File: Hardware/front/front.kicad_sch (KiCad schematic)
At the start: 31 parts, among them J101 Conn_02x10_Odd_Even, J102 Conn_02x08_Odd_Even, SW101 Alps EC11E, SW102 C&K-D6R-Illuminated, SW103 B3W-9002-Y1C, SW104 B3W-9002-Y1C, SW105 B3W-9002-Y1C, SW106 B3W-9002-Y1C, SW107 B3W-9000-RHG2C, U101 XRA1203, U102 AT24CS32-SSHM, U103 PCA9955B

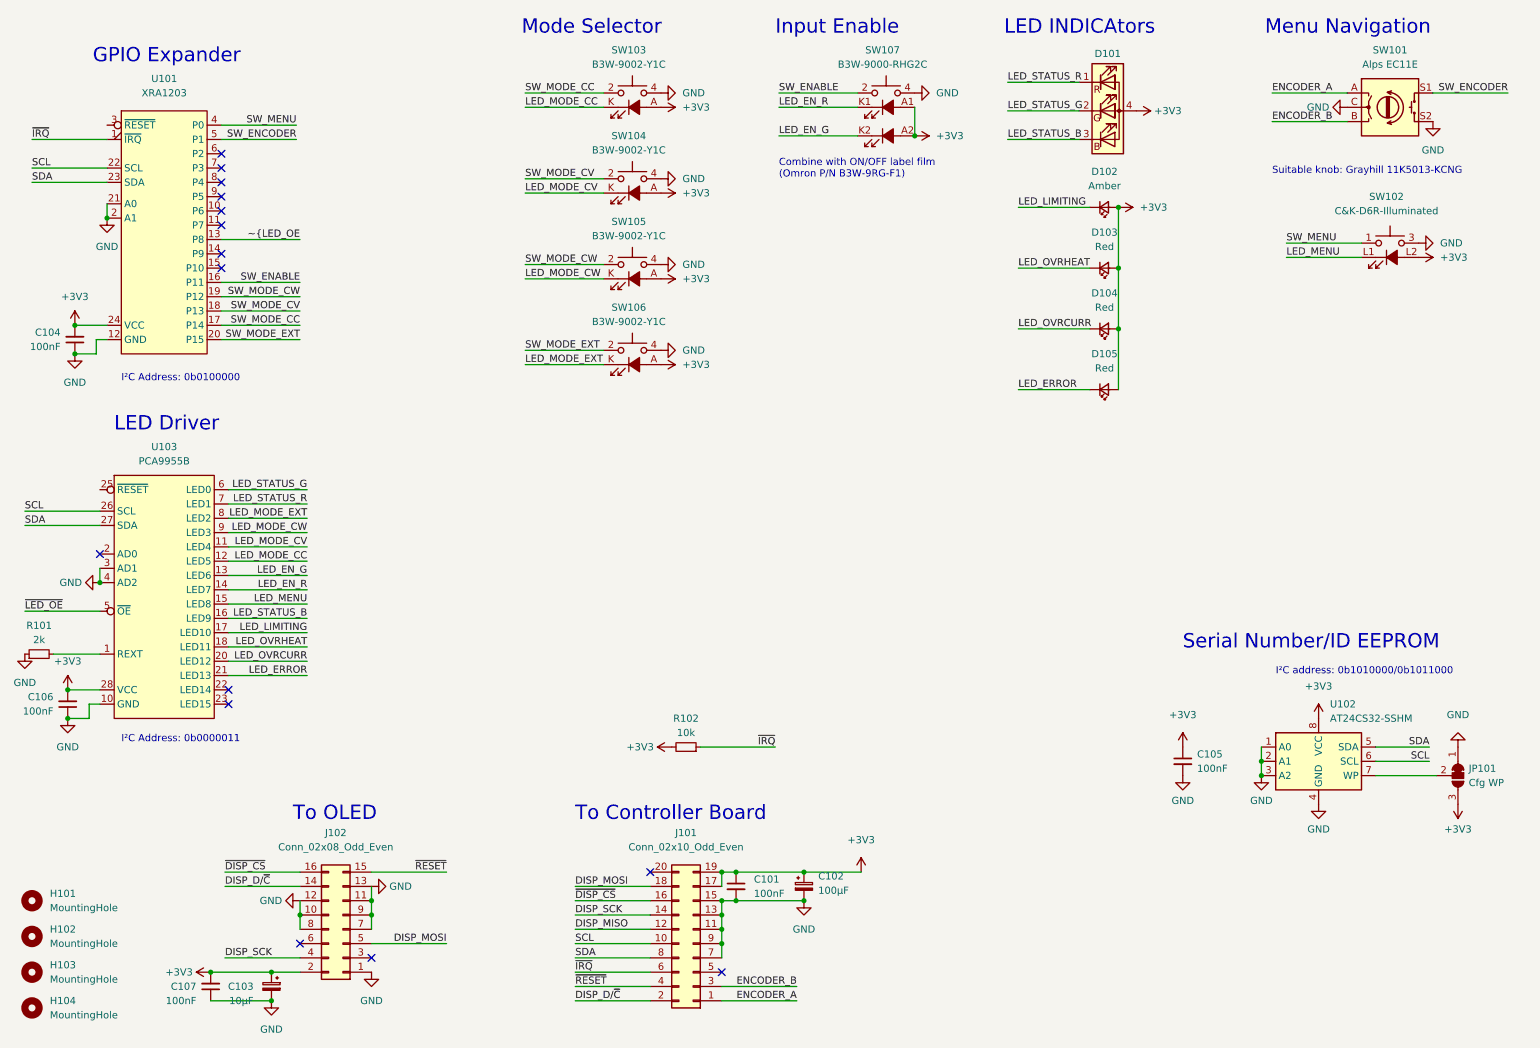
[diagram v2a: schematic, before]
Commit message: Tweaks to front and rear panel boards
- Minor movement of stuff and silkscreen cleanup for manufacturing
  exporting

- Removed display connector from front panel board; this is now directly
  connected to the controller instead, to make the board a bit simpler
  and reduce the amount of stuff going on
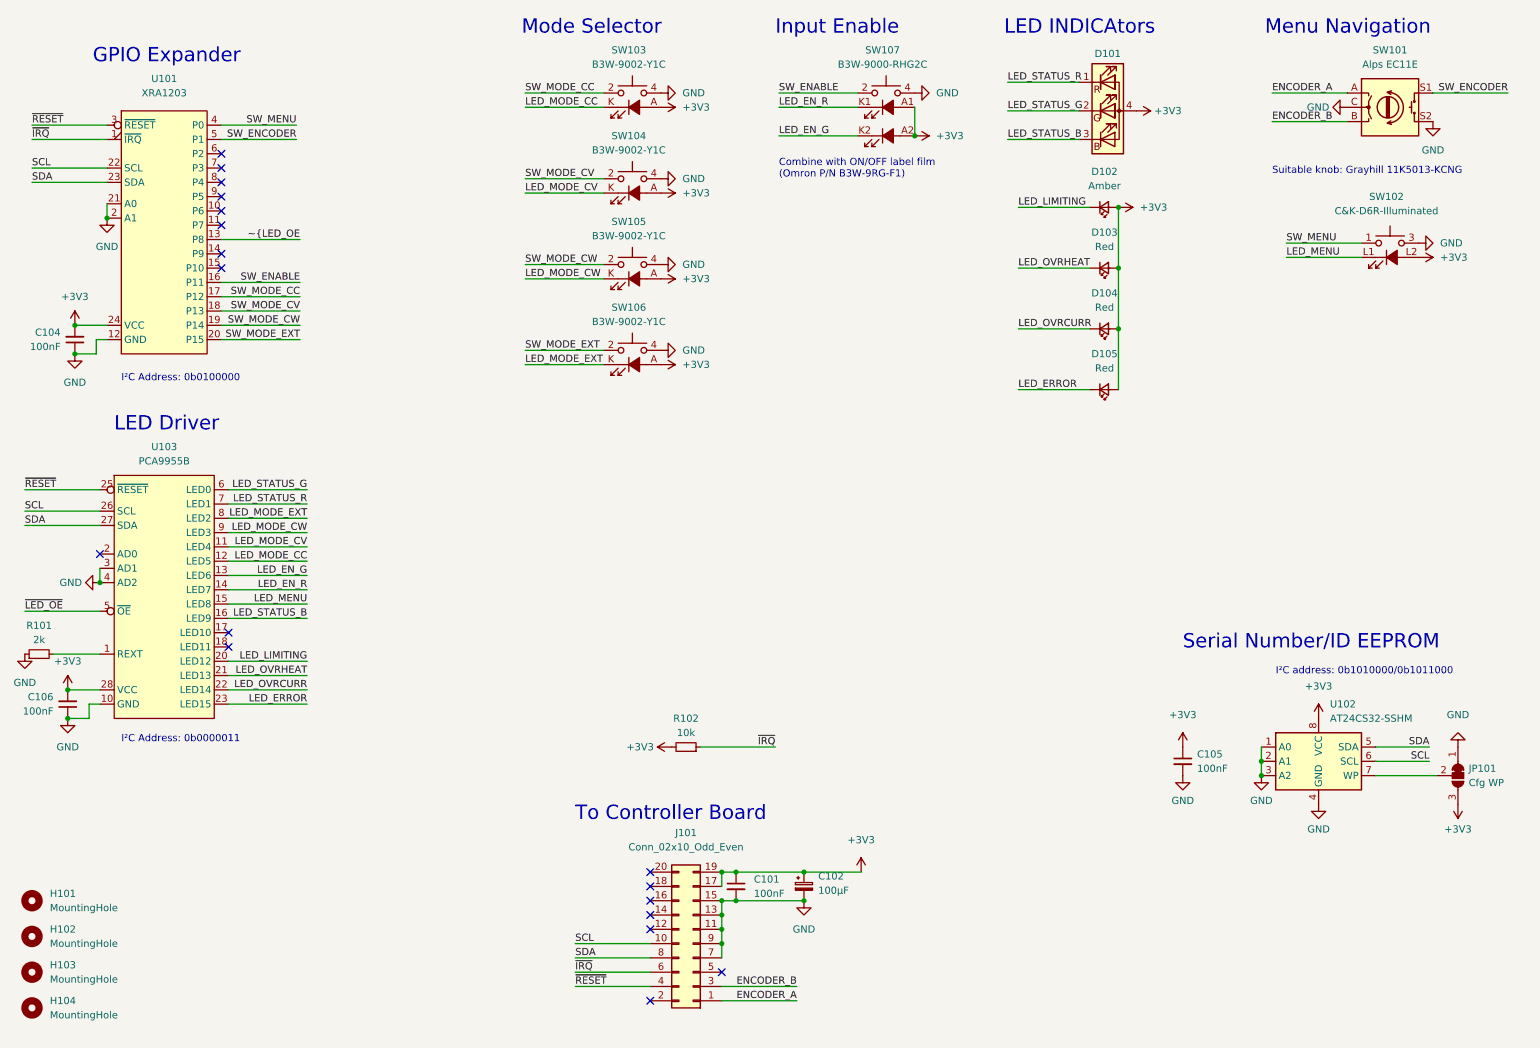
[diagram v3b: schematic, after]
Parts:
- removed C103: 10µF, Capacitor_Tantalum_SMD:CP_EIA-3216-18_Kemet-A_Pad1.58x1.35mm_HandSolder, symbol Device:C_Polarized_Small
- removed C107: 100nF, Capacitor_SMD:C_0805_2012Metric_Pad1.18x1.45mm_HandSolder, symbol Device:C_Small
- removed J102: Conn_02x08_Odd_Even, Connector_PinHeader_2.54mm:PinHeader_2x08_P2.54mm_Vertical_SMD, symbol Connector_Generic:Conn_02x08_Odd_Even
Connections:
- net LED_ERROR: now also U103.23 (LED15); no longer U103.21 (LED13)
- net LED_LIMITING: now also U103.20 (LED12); no longer U103.17 (LED10)
- net LED_OVRCURR: now also U103.22 (LED14); no longer U103.20 (LED12)
- net LED_OVRHEAT: now also U103.21 (LED13); no longer U103.18 (LED11)
- net ~{RESET}: now also U101.3 (~{RESET}), U103.25 (~{RESET})
- net DISP_D/~{C}: no longer names the net of J101.2 (Pin_2)
- net DISP_MISO: no longer names the net of J101.12 (Pin_12)
- net DISP_MOSI: no longer names the net of J101.18 (Pin_18)
- net DISP_SCK: no longer names the net of J101.14 (Pin_14)
- net ~{DISP_CS}: no longer names the net of J101.16 (Pin_16)
- no-connect marks 15 -> 18
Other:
- note removed: "To OLED"

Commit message: Rev 2 for front panel
- Adds debouncing for all switches on the board itself, and fixes the
  incorrect RGB LED footprint.

- Fix Omron B3W-9XXX switch footprints (they had soldermask over copper)
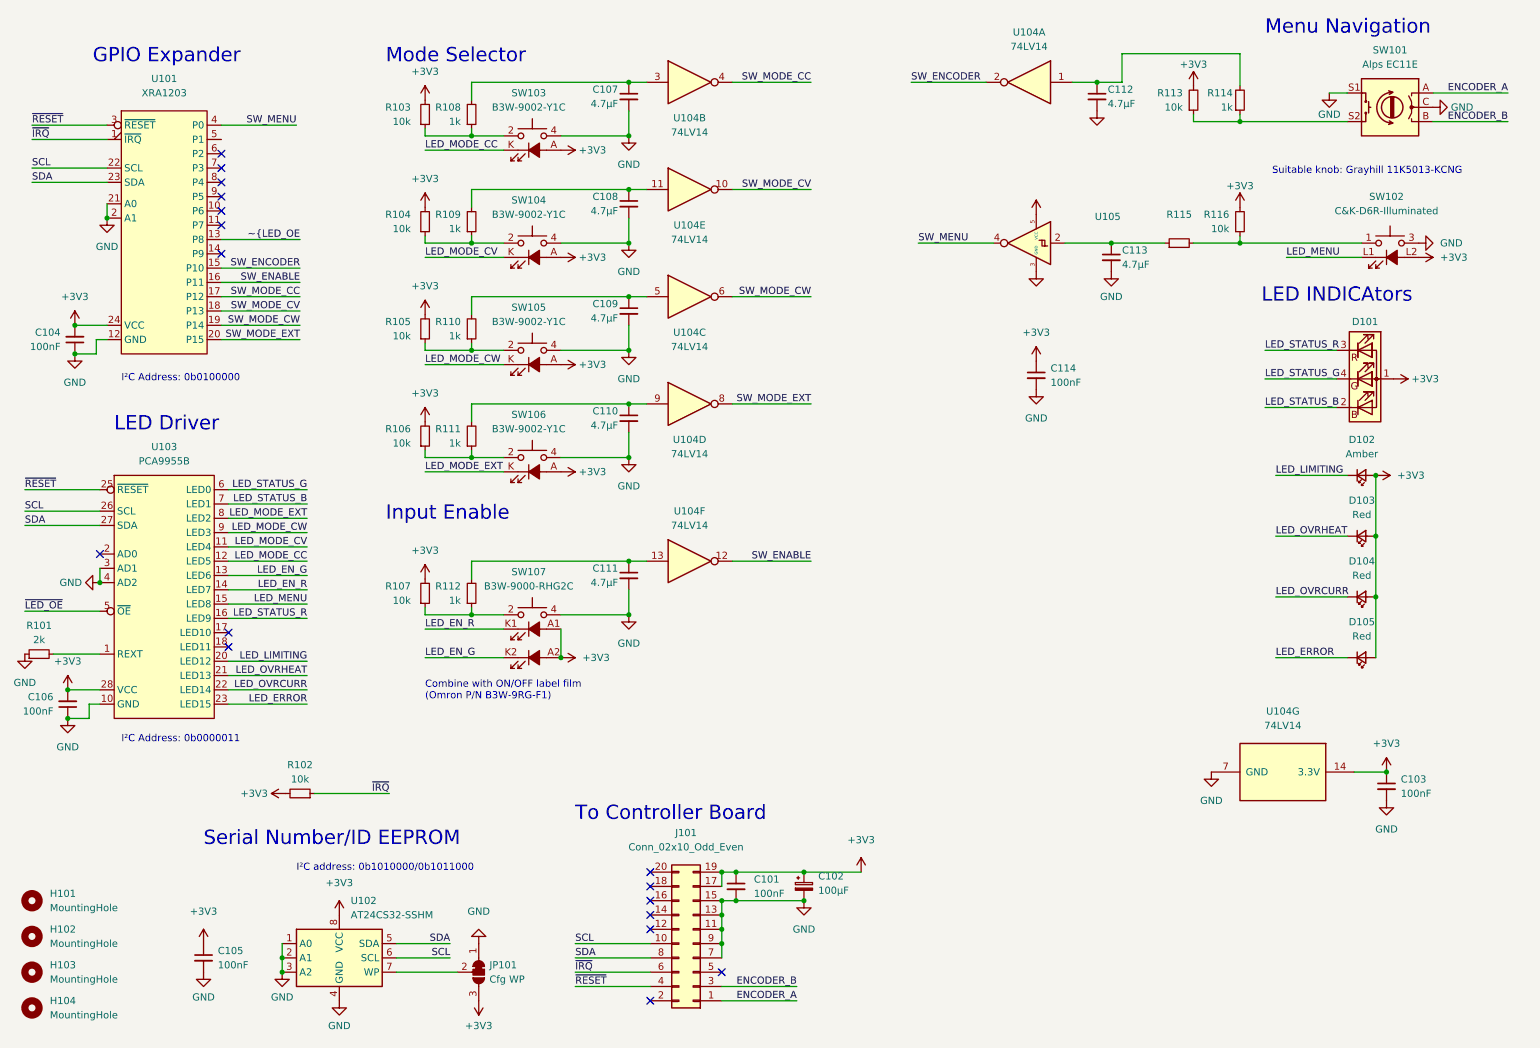
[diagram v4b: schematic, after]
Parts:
- added C103, C114: 100nF, Capacitor_SMD:C_0805_2012Metric_Pad1.18x1.45mm_HandSolder, symbol Device:C_Small
- added C107, C108, C109, C110, C111, C112, C113: 4.7µF, Capacitor_SMD:C_0805_2012Metric_Pad1.18x1.45mm_HandSolder, symbol Device:C_Small
- added R103, R104, R105, R106, R107, R113, R116: 10k, Resistor_SMD:R_0805_2012Metric_Pad1.20x1.40mm_HandSolder, symbol Device:R_Small
- added R108, R109, R110, R111, R112, R114: 1k, Resistor_SMD:R_0805_2012Metric_Pad1.20x1.40mm_HandSolder, symbol Device:R_Small
- added R115: (no value), symbol Device:R_Small
- added U104: 74LV14, Package_SO:TSSOP-14_4.4x5mm_P0.65mm, symbol 74xx:74LV14
- added U105: (no value), symbol 74xGxx:SN74LVC1G14DBV
- C105: MPN (none) -> CL21B104KACNFNC
- D101: symbol Device:LED_RGBA -> Device:LED_ABRG
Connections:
- net +3V3: now also D101.1 (A), C103.1, C114.1, R103.2, R104.2, R105.2, R106.2, R107.2, R113.2, R116.2, U104.14 (3.3V), U105.5 (VCC); no longer D101.4 (A)
- net GND: now also SW101.S1, C103.2, C107.2, C108.2, C109.2, C110.2, C111.2, C112.2, C113.2, C114.2, U104.7 (GND), U105.3 (GND); no longer SW101.S2
- net LED_STATUS_B: now also D101.2 (BK), U103.7 (LED1); no longer D101.3 (BK), U103.16 (LED9)
- net LED_STATUS_G: now also D101.4 (GK); no longer D101.2 (GK)
- net LED_STATUS_R: now also D101.3 (RK), U103.16 (LED9); no longer D101.1 (RK), U103.7 (LED1)
- net SW_ENABLE: now also U104.12; no longer SW107.1, SW107.2
- net SW_ENCODER: now also U101.15 (P10), U104.2; no longer SW101.S1, U101.5 (P1)
- net SW_MENU: now also U105.4; no longer SW102.1, SW102.2 (1)
- net SW_MODE_CC: now also U104.4; no longer SW103.1, SW103.2
- net SW_MODE_CV: now also U104.10; no longer SW104.1, SW104.2
- net SW_MODE_CW: now also U104.6; no longer SW105.1, SW105.2
- net SW_MODE_EXT: now also U104.8; no longer SW106.1, SW106.2
- new net: R103.1, R108.1, SW103.1, SW103.2
- new net: C111.1, R112.2, U104.13
- new net: R113.1, R114.1, SW101.S2
- new net: C112.1, R114.2, U104.1
- new net: C109.1, R110.2, U104.5
- new net: R104.1, R109.1, SW104.1, SW104.2
- new net: C108.1, R109.2, U104.11
- new net: R106.1, R111.1, SW106.1, SW106.2
- new net: C110.1, R111.2, U104.9
- new net: R107.1, R112.1, SW107.1, SW107.2
- new net: C113.1, R115.1, U105.2
- new net: R105.1, R110.1, SW105.1, SW105.2
- new net: R115.2, R116.1, SW102.1, SW102.2 (1)
- new net: C107.1, R108.2, U104.3
- no-connect marks 18 -> 17
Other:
- moved on the sheet: C105, D101, D102, D103, D104, D105, JP101, R102, SW103, SW104, SW105, SW106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
